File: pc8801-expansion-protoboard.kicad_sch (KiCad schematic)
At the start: 52 parts, among them J1 Solder Side, J10 CPOL select (to Fuji), J11 CPOL (Latch), J2 Parts Side, J3 5V, J4 12V, J5 -12V, J6 GND_1, J7 GND_2, J8 CPOL select (ESP)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

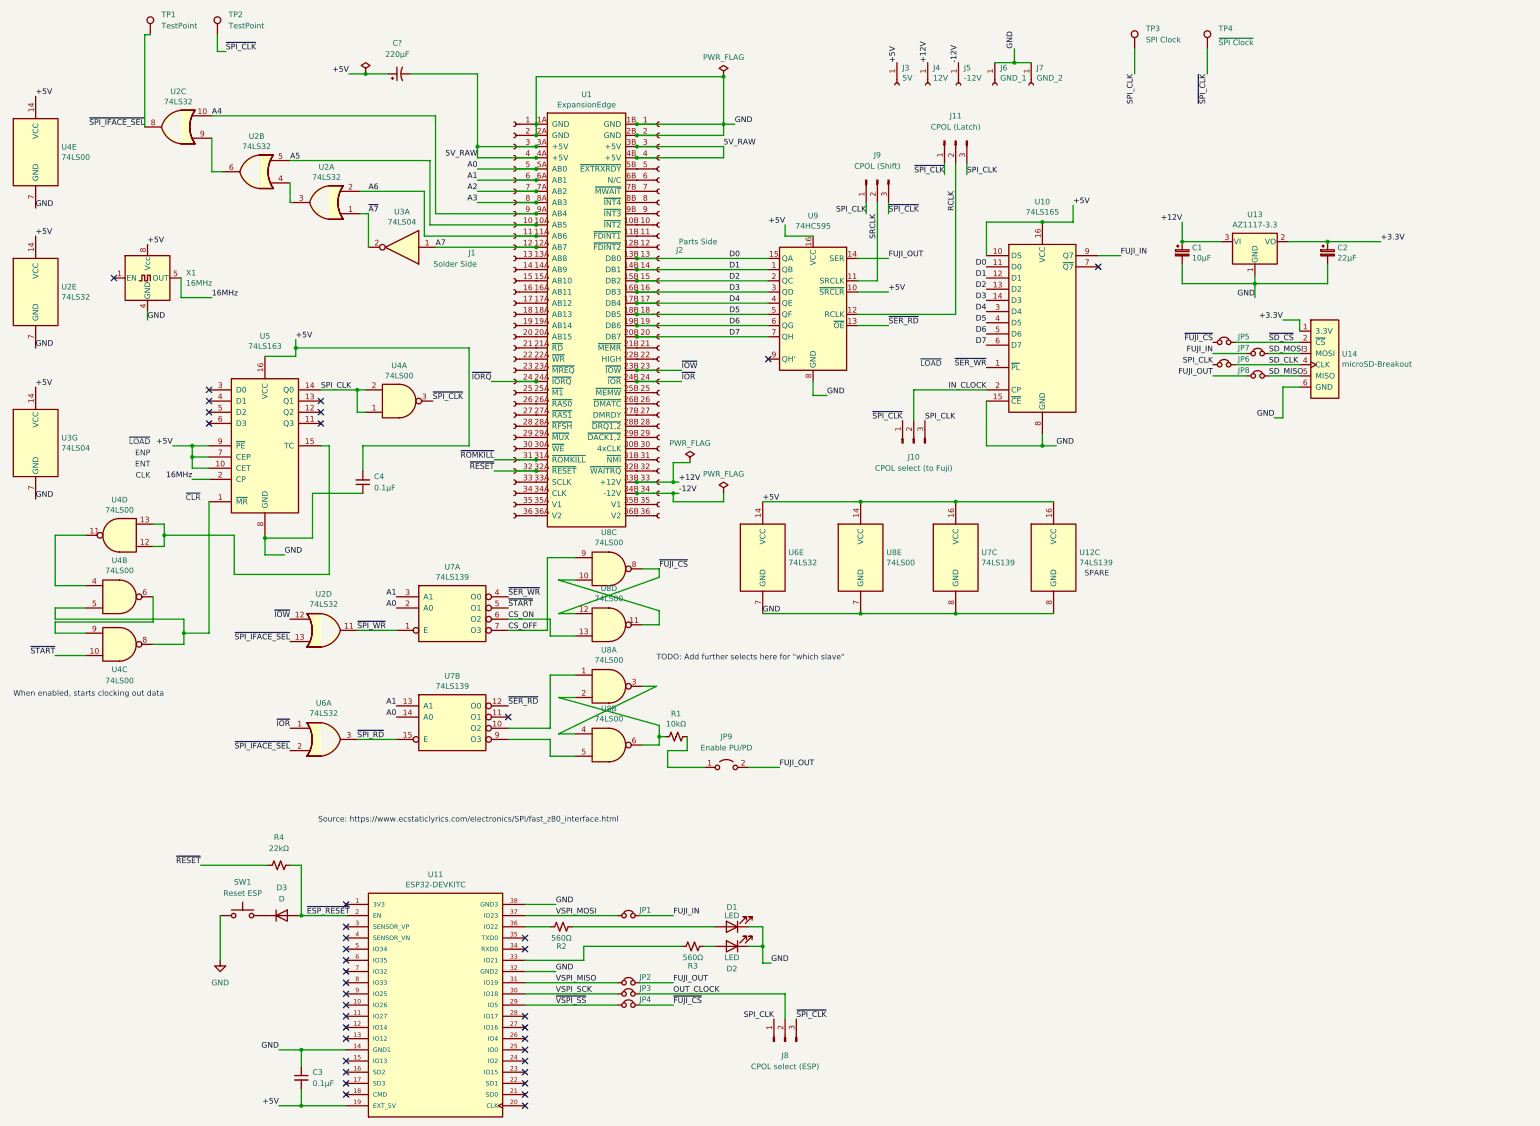
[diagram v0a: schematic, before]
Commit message: Place RP2040
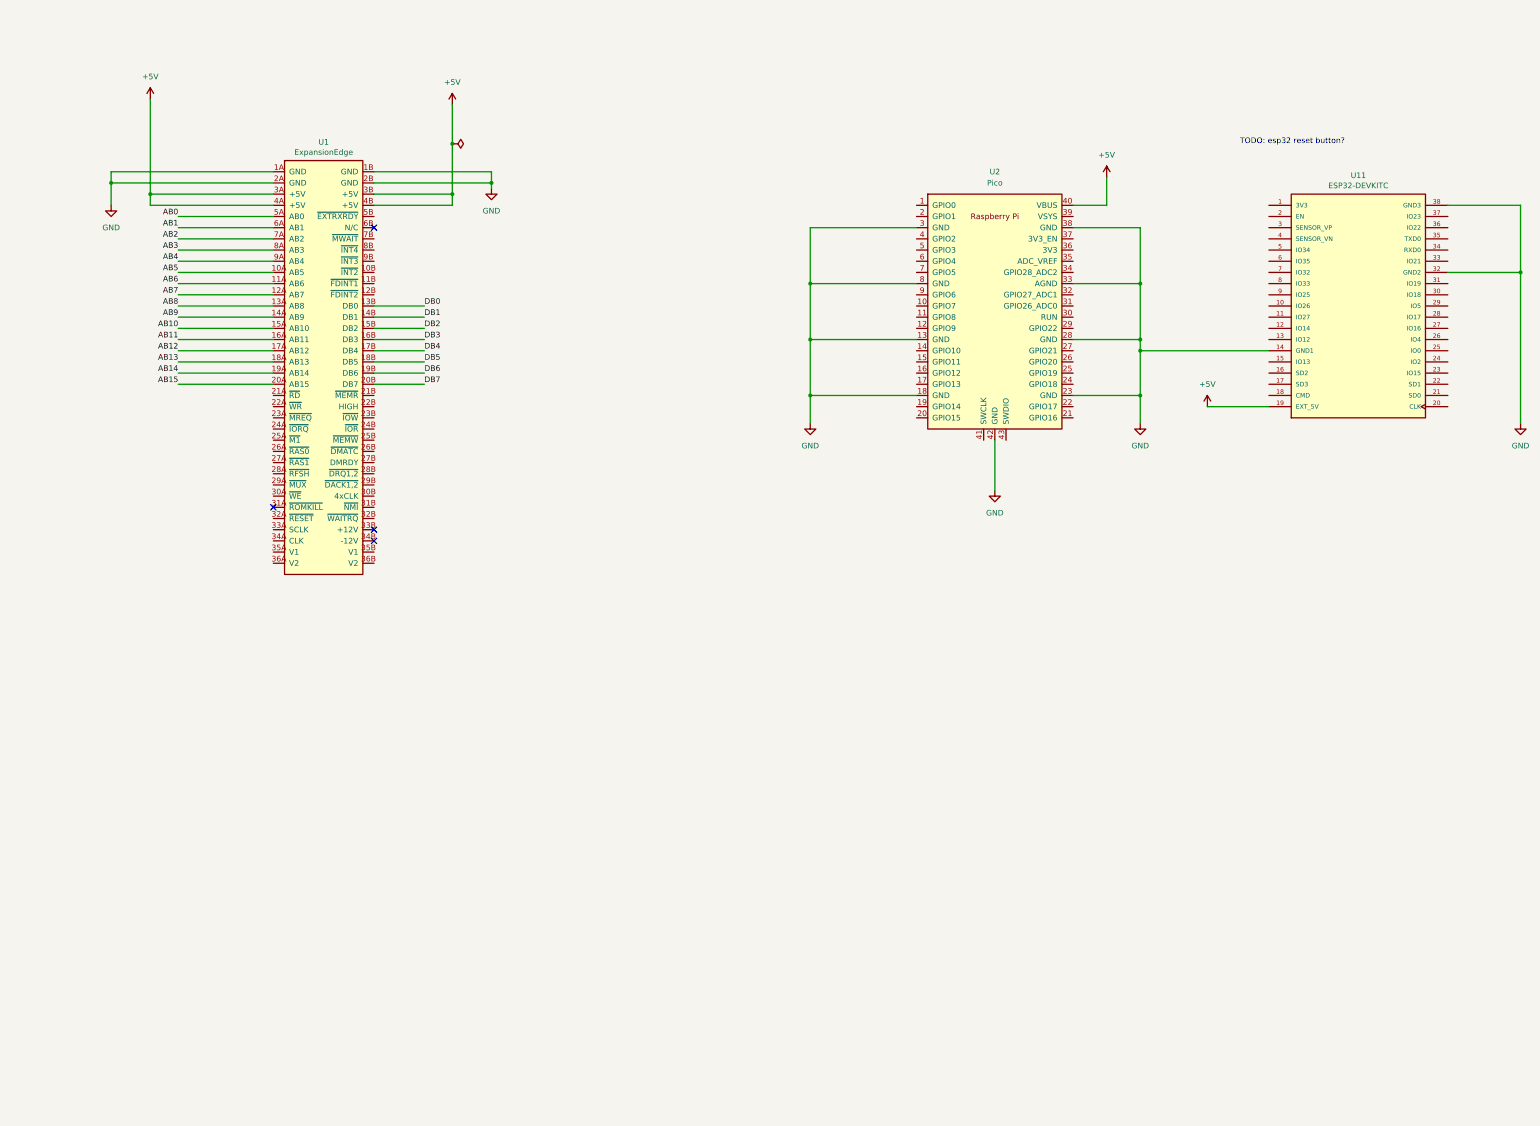
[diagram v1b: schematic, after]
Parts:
- removed C1: 10µF, Capacitor_THT:CP_Radial_D5.0mm_P2.00mm, symbol Device:CP_Small
- removed C2: 22µF, Capacitor_THT:CP_Radial_D5.0mm_P2.00mm, symbol Device:CP_Small
- removed C3, C4: 0.1µF, Capacitor_THT:C_Disc_D5.0mm_W2.5mm_P2.50mm, symbol Device:C_Small
- removed C?: 220µF, Capacitor_THT:CP_Radial_D5.0mm_P2.00mm, symbol Device:C_Polarized_Small_US
- removed D1, D2: LED, LED_THT:LED_D3.0mm, symbol Device:LED
- removed D3: D, Diode_THT:D_A-405_P10.16mm_Horizontal, symbol Device:D
- removed J1: Solder Side, Connector_PinHeader_2.54mm:PinHeader_1x36_P2.54mm_Vertical, symbol Connector:Conn_01x36_Female
- removed J10: CPOL select (to Fuji), Connector_PinHeader_2.54mm:PinHeader_1x03_P2.54mm_Vertical, symbol Connector:Conn_01x03_Male
- removed J11: CPOL (Latch), Connector_PinHeader_2.54mm:PinHeader_1x03_P2.54mm_Vertical, symbol Connector:Conn_01x03_Male
- removed J2: Parts Side, Connector_PinHeader_2.54mm:PinHeader_1x36_P2.54mm_Vertical, symbol Connector:Conn_01x36_Female
- removed J3: 5V, PC-8801:1x20_PowerBar, symbol Connector:Conn_01x01_Female
- removed J4: 12V, PC-8801:1x20_PowerBar, symbol Connector:Conn_01x01_Female
- removed J5: -12V, PC-8801:1x20_PowerBar, symbol Connector:Conn_01x01_Female
- removed J6: GND_1, PC-8801:1x20_PowerBar, symbol Connector:Conn_01x01_Female
- removed J7: GND_2, PC-8801:1x20_PowerBar, symbol Connector:Conn_01x01_Female
- removed J8: CPOL select (ESP), Connector_PinHeader_2.54mm:PinHeader_1x03_P2.54mm_Vertical, symbol Connector:Conn_01x03_Male
- removed J9: CPOL (Shift), Connector_PinHeader_2.54mm:PinHeader_1x03_P2.54mm_Vertical, symbol Connector:Conn_01x03_Male
- removed JP1, JP2, JP3, JP4, JP5, JP6, JP7, JP8: Jumper_NC_Small, Jumper:SolderJumper-2_P1.3mm_Bridged_RoundedPad1.0x1.5mm, symbol Device:Jumper_NC_Small
- removed JP9: Enable PU/PD, Connector_PinHeader_2.54mm:PinHeader_1x02_P2.54mm_Vertical, symbol Jumper:Jumper_2_Open
- removed R1: 10kΩ, Resistor_THT:R_Axial_DIN0207_L6.3mm_D2.5mm_P10.16mm_Horizontal, symbol Device:R_Small_US
- removed R2, R3: 560Ω, Resistor_THT:R_Axial_DIN0207_L6.3mm_D2.5mm_P10.16mm_Horizontal, symbol Device:R_Small_US
- removed R4: 22kΩ, Resistor_THT:R_Axial_DIN0207_L6.3mm_D2.5mm_P10.16mm_Horizontal, symbol Device:R_Small_US
- removed SW1: Reset ESP, Button_Switch_THT:SW_PUSH_6mm, symbol Switch:SW_Push
- removed TP1, TP2: TestPoint, TestPoint:TestPoint_Loop_D2.60mm_Drill1.4mm_Beaded, symbol Connector:TestPoint
- removed TP3: SPI Clock, TestPoint:TestPoint_Loop_D2.60mm_Drill1.4mm_Beaded, symbol Connector:TestPoint
- removed TP4: ~{SPI Clock}, TestPoint:TestPoint_Loop_D2.60mm_Drill1.4mm_Beaded, symbol Connector:TestPoint
- removed U10: 74LS165, Package_DIP:DIP-16_W7.62mm_Socket_LongPads, symbol 74xx:74LS165
- removed U12, U7: 74LS139, Package_DIP:DIP-16_W7.62mm_Socket_LongPads, symbol 74xx:74LS139
- removed U13: AZ1117-3.3, Package_TO_SOT_SMD:SOT-223, symbol Regulator_Linear:AZ1117-3.3
- removed U14: microSD-Breakout, microSD_Breakout:microSD_AliExpress, symbol microSD_Breakout:microSD-Breakout
- removed U2, U6: 74LS32, Package_DIP:DIP-14_W7.62mm_Socket_LongPads, symbol 74xx:74LS32
- removed U3: 74LS04, Package_DIP:DIP-14_W7.62mm_Socket_LongPads, symbol 74xx:74LS04
- removed U4, U8: 74LS00, Package_DIP:DIP-14_W7.62mm_Socket_LongPads, symbol 74xx:74LS00
- removed U5: 74LS163, Package_DIP:DIP-16_W7.62mm_Socket_LongPads, symbol 74xx:74LS163
- removed U9: 74HC595, Package_DIP:DIP-16_W7.62mm_Socket_LongPads, symbol 74xx:74HC595
- removed X1: 16MHz, Oscillator:Oscillator_DIP-8, symbol Oscillator:CXO_DIP8
- added U2: Pico, MCU_RaspberryPi_and_Boards:RPi_Pico_SMD_TH, symbol MCU_RaspberryPi_and_Boards:Pico
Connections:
- net 5V_RAW is gone; now on net +5V: U1.3A (+5V), U1.3B (+5V), U1.4A (+5V), U1.4B (+5V)
- net +5V: now also U2.40 (VBUS)
- net GND: now also U2.13 (GND), U2.18 (GND), U2.23 (GND), U2.28 (GND), U2.3 (GND), U2.33 (AGND), U2.38 (GND), U2.42 (GND), U2.8 (GND)
- net AB8: now reaches U1.13A (AB8)
- net AB9: now reaches U1.14A (AB9)
- net AB10: now reaches U1.15A (AB10)
- net AB11: now reaches U1.16A (AB11)
- net AB12: now reaches U1.17A (AB12)
- net AB13: now reaches U1.18A (AB13)
- net AB14: now reaches U1.19A (AB14)
- net AB15: now reaches U1.20A (AB15)
- net +12V: no longer names the net of U1.33B (+12V)
- net -12V: no longer names the net of U1.34B (-12V)
- net A0 renamed AB0
- net A1 renamed AB1
- net A2 renamed AB2
- net A3 renamed AB3
- net A4 renamed AB4
- net A5 renamed AB5
- net A6 renamed AB6
- net A7 renamed AB7
- net D0 renamed DB0
- net D1 renamed DB1
- net D2 renamed DB2
- net D3 renamed DB3
- net D4 renamed DB4
- net D5 renamed DB5
- net D6 renamed DB6
- net D7 renamed DB7
- net VSPI_MISO: no longer names the net of U11.31 (IO19)
- net VSPI_MOSI: no longer names the net of U11.37 (IO23)
- net VSPI_SCK: no longer names the net of U11.30 (IO18)
- net ~{ESP_RESET}: no longer names the net of U11.2 (EN)
- net ~{IORQ}: no longer names the net of U1.24A (~{IORQ})
- net ~{IOR}: no longer names the net of U1.24B (~{IOR})
- net ~{IOW}: no longer names the net of U1.23B (~{IOW})
- net ~{RESET}: no longer names the net of U1.32A (~{RESET})
- net ~{ROMKILL}: no longer names the net of U1.31A (~{ROMKILL})
- net ~{VSPI_SS}: no longer names the net of U11.29 (IO5)
- no-connect marks 38 -> 4
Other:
- note added: "TODO: esp32 reset button?"
- note removed: "CLK"
- note removed: "ENP"
- note removed: "ENT"
- note removed: "SPARE"
- note removed: "Source: https://www.ecstaticlyrics.com/electronics/SPI/fast_z80_interface.html"
- note removed: "TODO: Add further selects here for "which slave""
- note removed: "When enabled, starts clocking out data"
- note removed: "~{CLR}"
- note removed: "~{LOAD}"
- moved on the sheet: U1, U11

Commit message: Mocking out Mozzwald's design
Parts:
- removed U2: Pico, MCU_RaspberryPi_and_Boards:RPi_Pico_SMD_TH, symbol MCU_RaspberryPi_and_Boards:Pico
- added C1: 4.7µF, symbol Device:C_Polarized_Small_US
- added D1: 1n5817, symbol Device:D_Zener
- added J1: SD card, microSD_Breakout:microSD_AliExpress, symbol Connector:Conn_01x06_Pin
- added R1, R2, R6: 10kΩ, symbol Device:R_Small_US
- added SW1: Reset ESP, Button_Switch_THT:SW_PUSH_6mm, symbol Switch:SW_Push
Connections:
- net +5V: no longer U1.3B (+5V), U1.4B (+5V), U11.19 (EXT_5V)
- net GND: now also C1.2, J1.6 (Pin_6), SW1.2
- net ESP_3v3: now reaches U11.1 (3V3)
- net ESP_3v3: now also C1.1, J1.1 (Pin_1), R1.1, R2.1, R6.1
- net PROC: now reaches U11.10 (IO26)
- net INT: now reaches U11.11 (IO27)
- net ~{ESP_RESET}: now reaches U11.2 (EN)
- net ~{ESP_RESET}: now also SW1.1
- net WIFI_LED: now reaches U11.24 (IO2)
- net io0: now reaches U11.25 (IO0)
- net BUS_LED: now reaches U11.26 (IO4)
- net ~{SPI_CS}: now reaches U11.29 (IO5)
- net ~{SPI_CS}: now also J1.2 (Pin_2), R2.2
- net SPI_CLK: now reaches U11.30 (IO18)
- net SPI_CLK: now also J1.4 (Pin_4)
- net SPI_MISO: now reaches U11.31 (IO19)
- net SPI_MISO: now also J1.5 (Pin_5), R1.2
- net ESP_RX: now reaches U11.34 (RXD0)
- net ESP_TX: now reaches U11.35 (TXD0)
- net SPI_MOSI: now reaches U11.37 (IO23)
- net SPI_MOSI: now also J1.3 (Pin_3), R6.2
- net CMD: now reaches U11.9 (IO25)
- new net: D1.1 (K), U11.19 (EXT_5V)
- new net PC88_5V: D1.2 (A), U1.3B (+5V), U1.4B (+5V)
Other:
- note added: "TODO: Put purple pico on"
- note removed: "TODO: esp32 reset button?"

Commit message: LEDs
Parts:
- added D2: Bus LED, LED_THT:LED_D3.0mm, symbol Device:LED
- added D3: Wifi LED, LED_THT:LED_D3.0mm, symbol Device:LED
- added R3, R4: 1kΩ, symbol Device:R_Small_US
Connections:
- net BUS_LED: now also D2.2 (A)
- net GND: now also R3.2, R4.2
- net WIFI_LED: now also D3.2 (A)
- new net: D3.1 (K), R4.1
- new net: D2.1 (K), R3.1
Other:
- note added: "Orange"
- note added: "White"
